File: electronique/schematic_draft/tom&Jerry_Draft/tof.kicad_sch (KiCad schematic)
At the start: 3 parts, among them U701 VL53L1CXV0FY1

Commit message: KiCAD V3 - 18.09.2024
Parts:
- renumbered C701 to C1201, C702 to C1202, U701 to U1201
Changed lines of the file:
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@@
+	(wire
+		(pts
+			(xy 119.38 69.85) (xy 121.92 69.85)
+		)
+		(stroke
+			(width 0)
+			(type default)
+		)
+	)
 	(wire
 		(pts
@@
 		(dnp no)
 		(fields_autoplaced yes)
-		(property "Reference" "C702"
+		(property "Reference" "C1202"
 			(at 124.4599 76.2 0)
 			(effects
@@
 	(symbol
 		(lib_id "power:GND")
-		(at 121.92 69.85 270)
+		(at 119.38 69.85 270)
 		(mirror x)
 		(unit 1)
@@
 		(dnp no)
 		(fields_autoplaced yes)
-		(property "Reference" "#PWR0702"
-			(at 115.57 69.85 0)
+		(property "Reference" "#PWR01202"
+			(at 113.03 69.85 0)
 			(effects
 				(font
@@
 		)
 		(property "Value" "GND"
-			(at 118.11 69.8499 90)
+			(at 115.57 69.8499 90)
 			(effects
 				(font
@@
 		)
 		(property "Footprint" ""
-			(at 121.92 69.85 0)
+			(at 119.38 69.85 0)
 			(effects
 				(font
@@
 		)
 		(property "Datasheet" ""
-			(at 121.92 69.85 0)
+			(at 119.38 69.85 0)
 			(effects
 				(font
@@
 		)
 		(property "Description" "Power symbol creates a global label with name \"GND\" , ground"
-			(at 121.92 69.85 0)
+			(at 119.38 69.85 0)
 			(effects
 				(font
@@
 		(dnp no)
 		(fields_autoplaced yes)
-		(property "Reference" "#PWR0701"
+		(property "Reference" "#PWR01201"
 			(at 125.73 66.04 0)
 			(effects
@@
 		(on_board yes)
 		(dnp no)
-		(property "Reference" "C701"
+		(property "Reference" "C1201"
 			(at 123.444 60.96 0)
 			(effects
@@
 		(dnp no)
 		(fields_autoplaced yes)
-		(property "Reference" "#PWR0703"
+		(property "Reference" "#PWR01203"
 			(at 146.05 106.68 0)
 			(effects
@@
 		(dnp no)
 		(fields_autoplaced yes)
-		(property "Reference" "U701"
+		(property "Reference" "U1201"
 			(at 129.54 87.6299 0)
 			(effects

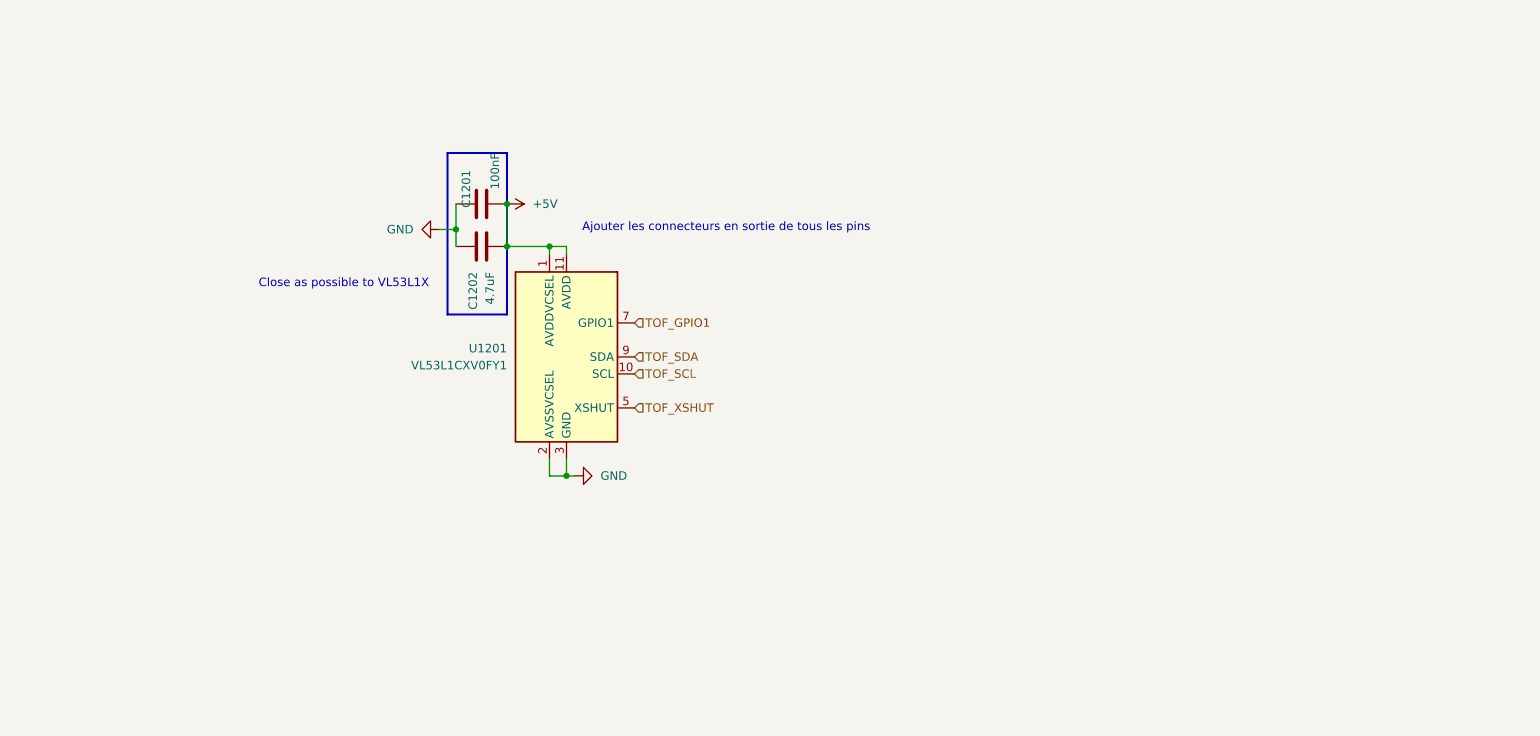
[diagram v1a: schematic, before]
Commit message: STM32 KiCAD V5 - 25.09.2024 - Ajout connecteurs TOF, ...
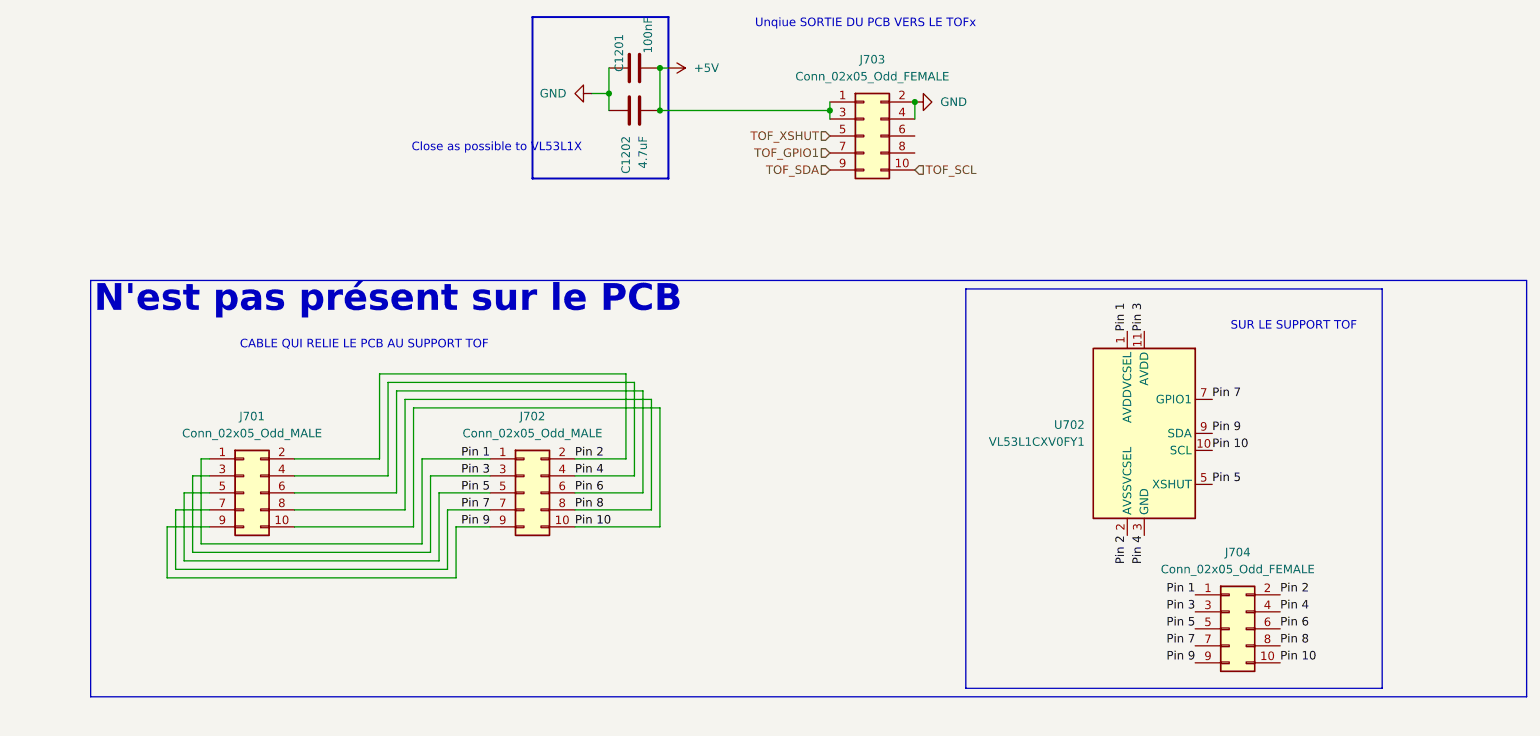
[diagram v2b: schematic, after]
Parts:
- removed U1201: VL53L1CXV0FY1, Sensor_Distance:ST_VL53L1x, symbol Sensor_Distance:VL53L1CXV0FY1
- added J701, J702: Conn_02x05_Odd_MALE, symbol Connector_Generic:Conn_02x05_Odd_Even
- added J703, J704: Conn_02x05_Odd_FEMALE, symbol Connector_Generic:Conn_02x05_Odd_Even
- added U702: VL53L1CXV0FY1, Sensor_Distance:ST_VL53L1x, symbol Sensor_Distance:VL53L1CXV0FY1
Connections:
- net +5V: now also J703.1 (Pin_1), J703.3 (Pin_3)
- net GND: now also J703.2 (Pin_2), J703.4 (Pin_4)
- net TOF_GPIO1: now also J703.7 (Pin_7)
- net TOF_SCL: now also J703.10 (Pin_10)
- net TOF_SDA: now also J703.9 (Pin_9)
- net TOF_XSHUT: now also J703.5 (Pin_5)
- new net Pin 1: J701.1 (Pin_1), J702.1 (Pin_1), J704.1 (Pin_1), U702.1 (AVDDVCSEL)
- new net Pin 10: J701.10 (Pin_10), J702.10 (Pin_10), J704.10 (Pin_10), U702.10 (SCL)
- new net Pin 2: J701.2 (Pin_2), J702.2 (Pin_2), J704.2 (Pin_2), U702.2 (AVSSVCSEL)
- new net Pin 3: J701.3 (Pin_3), J702.3 (Pin_3), J704.3 (Pin_3), U702.11 (AVDD)
- new net Pin 4: J701.4 (Pin_4), J702.4 (Pin_4), J704.4 (Pin_4), U702.12 (GND), U702.3 (GND), U702.4 (GND), U702.6 (GND)
- new net Pin 5: J701.5 (Pin_5), J702.5 (Pin_5), J704.5 (Pin_5), U702.5 (XSHUT)
- new net Pin 6: J701.6 (Pin_6), J702.6 (Pin_6), J704.6 (Pin_6)
- new net Pin 7: J701.7 (Pin_7), J702.7 (Pin_7), J704.7 (Pin_7), U702.7 (GPIO1)
- new net Pin 8: J701.8 (Pin_8), J702.8 (Pin_8), J704.8 (Pin_8)
- new net Pin 9: J701.9 (Pin_9), J702.9 (Pin_9), J704.9 (Pin_9), U702.9 (SDA)
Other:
- note added: "CABLE QUI RELIE LE PCB AU SUPPORT TOF"
- note added: "N'est pas présent sur le PCB"
- note added: "SUR LE SUPPORT TOF"
- note added: "Unqiue SORTIE DU PCB VERS LE TOFx"
- note removed: "Ajouter les connecteurs en sortie de tous les pins"
- moved on the sheet: C1201, C1202

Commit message: STM32 KiCAD V6 - 25.09.2024 - Ajout des points test
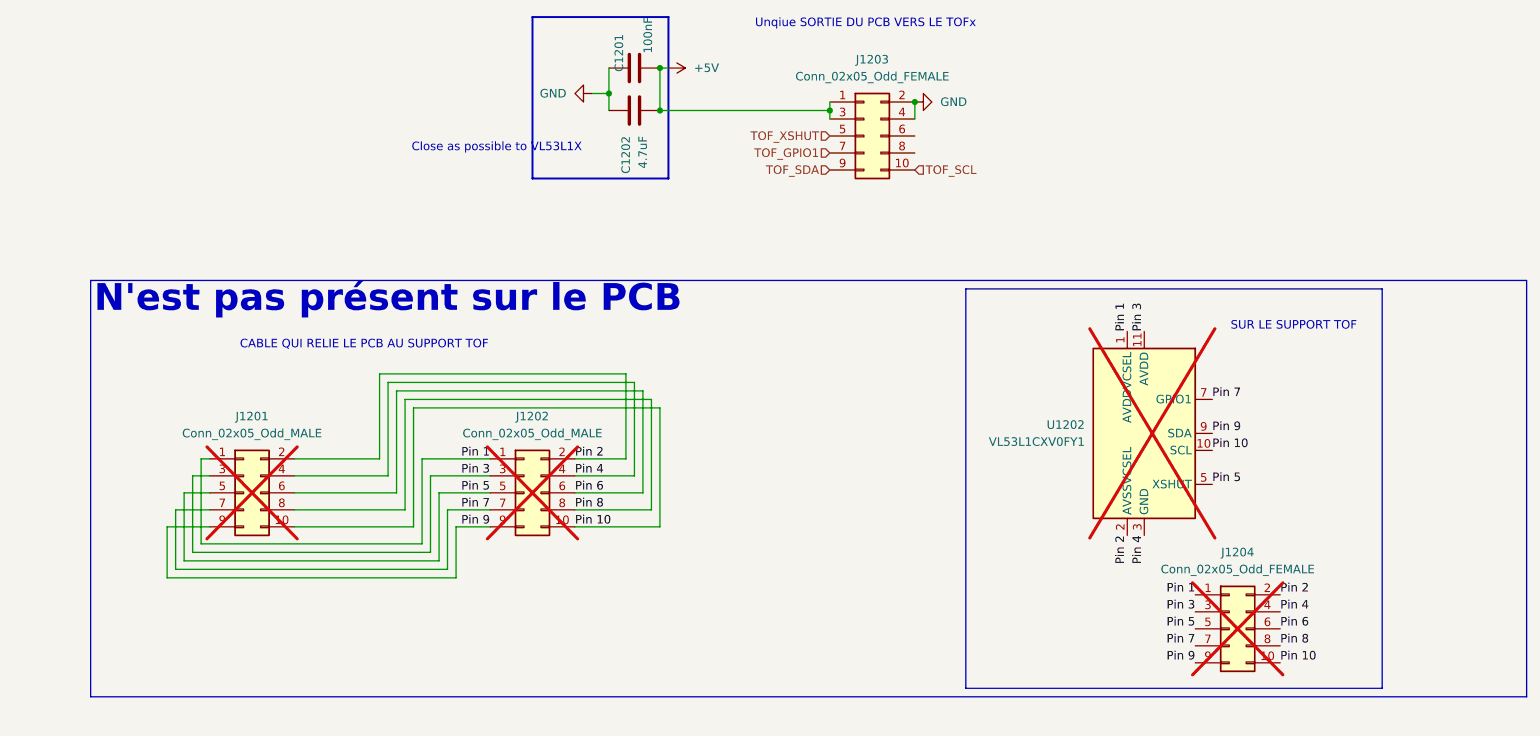
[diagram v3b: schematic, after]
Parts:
- J1201: renamed from J701; now not fitted
- J1202: renamed from J702; now not fitted
- J1204: renamed from J704; now not fitted
- U1202: renamed from U702; now not fitted
- renumbered J703 to J1203
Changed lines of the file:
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@@
 		(exclude_from_sim no)
 		(in_bom yes)
-		(on_board yes)
-		(dnp no)
-		(property "Reference" "U702"
+		(on_board no)
+		(dnp yes)
+		(property "Reference" "U1202"
 			(at 215.9 99.0599 0)
 			(effects
@@
 		(exclude_from_sim no)
 		(in_bom yes)
-		(on_board yes)
-		(dnp no)
-		(property "Reference" "J704"
+		(on_board no)
+		(dnp yes)
+		(property "Reference" "J1204"
 			(at 238.76 118.11 0)
 			(effects
@@
 		(dnp no)
 		(fields_autoplaced yes)
-		(property "Reference" "#PWR0704"
+		(property "Reference" "#PWR01204"
 			(at 196.85 50.8 0)
 			(effects
@@
 		(on_board yes)
 		(dnp no)
-		(property "Reference" "J703"
+		(property "Reference" "J1203"
 			(at 184.15 44.45 0)
 			(effects
@@
 		(exclude_from_sim no)
 		(in_bom yes)
-		(on_board yes)
-		(dnp no)
-		(property "Reference" "J702"
+		(on_board no)
+		(dnp yes)
+		(property "Reference" "J1202"
 			(at 133.35 97.79 0)
 			(effects
@@
 		(exclude_from_sim no)
 		(in_bom yes)
-		(on_board yes)
-		(dnp no)
-		(property "Reference" "J701"
+		(on_board no)
+		(dnp yes)
+		(property "Reference" "J1201"
 			(at 91.44 97.79 0)
 			(effects
